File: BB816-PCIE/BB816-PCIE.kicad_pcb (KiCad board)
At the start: 4 copper layers, 167.6 x 111.2 mm, 2 parts, among them J1 BB816_BreakoutA27_PCIex16, J2 BB816_Breakout_A27

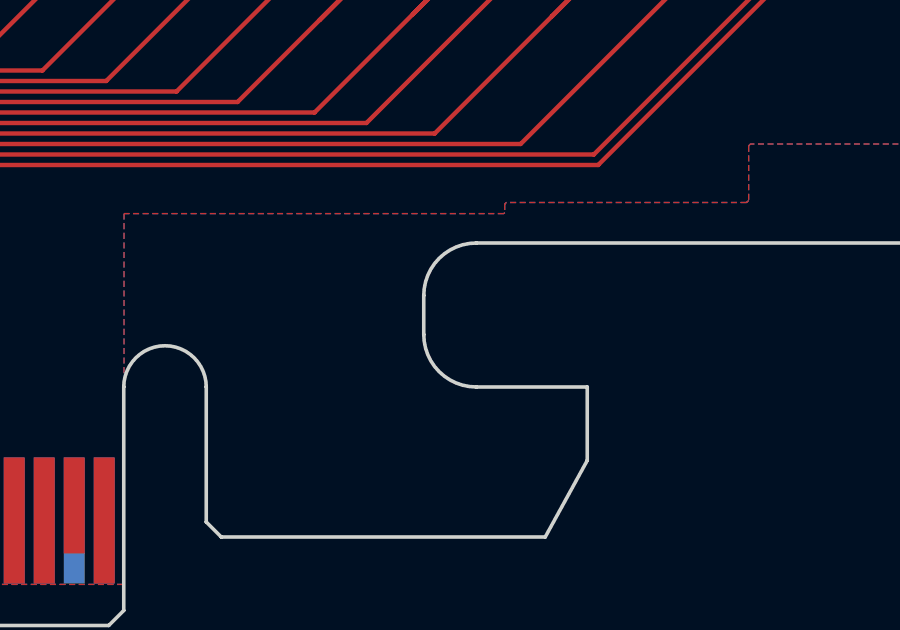
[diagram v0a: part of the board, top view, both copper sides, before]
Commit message: Add VIA and ACIA
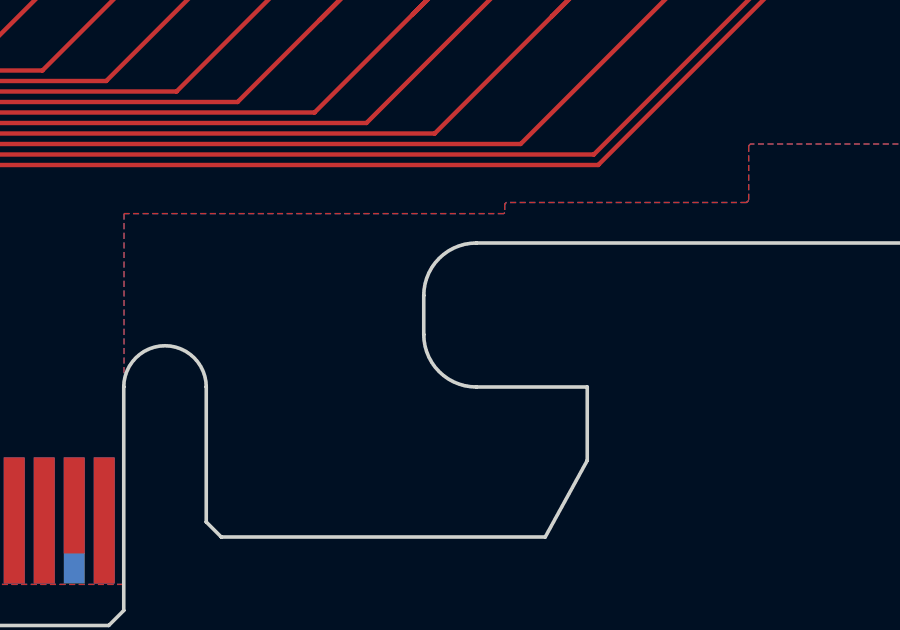
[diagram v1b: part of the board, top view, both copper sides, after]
